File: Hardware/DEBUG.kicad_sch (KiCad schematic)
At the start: 0 parts

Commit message: Checkpoint
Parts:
- added J11: STDC14, leptunKicadLib:FTSH-107-01-L-DV-K-A, symbol Connector_Generic:Conn_02x07_Odd_Even
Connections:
- new net GND: J11.5 (Pin_5), J11.7 (Pin_7)
- new net T_JCLK/T_SWCLK: J11.6 (Pin_6), J11.9 (Pin_9)
- new net T_JTDI: J11.10 (Pin_10)
- new net T_JTDO/T_SWO: J11.8 (Pin_8)
- new net T_JTMS/T_SWDIO: J11.4 (Pin_4)
- new net T_NRST : J11.12 (Pin_12)
- new net T_VCC: J11.3 (Pin_3)
- new net T_VCP_RX: J11.13 (Pin_13)
- new net T_VCP_TX: J11.14 (Pin_14)
- no-connect marks 0 -> 3
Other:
- note added: "GNDDetect"
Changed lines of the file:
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@@
 (kicad_sch (version 20230121) (generator eeschema)
   (paper "A4")
-  (hierarchical_label "SWCLK" (shape bidirectional) (at 101.6 83.82 0) (fields_autoplaced)
+  (junction (at 154.94 91.44) (diameter 0) (color 0 0 0 0)
+  )
+  (junction (at 137.16 93.98) (diameter 0) (color 0 0 0 0)
+  )
+  (no_connect (at 124.46 99.06))
+  (no_connect (at 152.4 86.36))
+  (no_connect (at 139.7 86.36))
+  (wire (pts (xy 134.62 101.6) (xy 139.7 101.6))
+    (stroke (width 0) (type default))
+  )
+  (wire (pts (xy 137.16 91.44) (xy 139.7 91.44))
+    (stroke (width 0) (type default))
+  )
+  (wire (pts (xy 157.48 96.52) (xy 152.4 96.52))
+    (stroke (width 0) (type default))
+  )
+  (wire (pts (xy 137.16 93.98) (xy 139.7 93.98))
+    (stroke (width 0) (type default))
+  )
+  (wire (pts (xy 154.94 91.44) (xy 152.4 91.44))
+    (stroke (width 0) (type default))
+  )
+  (wire (pts (xy 157.48 91.44) (xy 154.94 91.44))
+    (stroke (width 0) (type default))
+  )
+  (wire (pts (xy 137.16 91.44) (xy 137.16 93.98))
+    (stroke (width 0) (type default))
+  )
+  (wire (pts (xy 124.46 99.06) (xy 139.7 99.06))
+    (stroke (width 0) (type default))
+  )
+  (wire (pts (xy 157.48 99.06) (xy 152.4 99.06))
+    (stroke (width 0) (type default))
+  )
+  (wire (pts (xy 134.62 93.98) (xy 137.16 93.98))
+    (stroke (width 0) (type default))
+  )
+  (wire (pts (xy 157.48 101.6) (xy 152.4 101.6))
+    (stroke (width 0) (type default))
+  )
+  (wire (pts (xy 137.16 104.14) (xy 154.94 104.14))
+    (stroke (width 0) (type default))
+  )
+  (wire (pts (xy 157.48 88.9) (xy 152.4 88.9))
+    (stroke (width 0) (type default))
+  )
+  (wire (pts (xy 139.7 96.52) (xy 137.16 96.52))
+    (stroke (width 0) (type default))
+  )
+  (wire (pts (xy 157.48 93.98) (xy 152.4 93.98))
+    (stroke (width 0) (type default))
+  )
+  (wire (pts (xy 137.16 96.52) (xy 137.16 104.14))
+    (stroke (width 0) (type default))
+  )
+  (wire (pts (xy 154.94 104.14) (xy 154.94 91.44))
+    (stroke (width 0) (type default))
+  )
+  (wire (pts (xy 134.62 88.9) (xy 139.7 88.9))
+    (stroke (width 0) (type default))
+  )
+  (text "GNDDetect" (at 124.46 99.06 0)
+    (effects (font (size 1.27 1.27)) (justify left bottom))
+  )
+  (hierarchical_label "T_JTMS{slash}T_SWDIO" (shape bidirectional) (at 157.48 88.9 0) (fields_autoplaced)
     (effects (font (size 1.27 1.27)) (justify left))
   )
-  (hierarchical_label "~{NRST}" (shape bidirectional) (at 101.6 78.74 0) (fields_autoplaced)
+  (hierarchical_label "T_JTDO{slash}T_SWO" (shape input) (at 157.48 93.98 0) (fields_autoplaced)
     (effects (font (size 1.27 1.27)) (justify left))
   )
-  (hierarchical_label "VCP_TX" (shape output) (at 101.6 88.9 0) (fields_autoplaced)
+  (hierarchical_label "T_NRST " (shape bidirectional) (at 157.48 99.06 0) (fields_autoplaced)
     (effects (font (size 1.27 1.27)) (justify left))
   )
-  (hierarchical_label "VCP_RX" (shape input) (at 101.6 91.44 0) (fields_autoplaced)
+  (hierarchical_label "T_VCC" (shape passive) (at 134.62 88.9 180) (fields_autoplaced)
+    (effects (font (size 1.27 1.27)) (justify right))
+  )
+  (hierarchical_label "T_JCLK{slash}T_SWCLK" (shape output) (at 157.48 91.44 0) (fields_autoplaced)
     (effects (font (size 1.27 1.27)) (justify left))
   )
-  (hierarchical_label "SWDIO" (shape bidirectional) (at 101.6 81.28 0) (fields_autoplaced)
+  (hierarchical_label "T_VCP_TX" (shape input) (at 157.48 101.6 0) (fields_autoplaced)
     (effects (font (size 1.27 1.27)) (justify left))
   )
-  (hierarchical_label "SWO" (shape bidirectional) (at 101.6 86.36 0) (fields_autoplaced)
+  (hierarchical_label "T_VCP_RX" (shape output) (at 134.62 101.6 180) (fields_autoplaced)
+    (effects (font (size 1.27 1.27)) (justify right))
+  )
+  (hierarchical_label "T_JTDI" (shape output) (at 157.48 96.52 0) (fields_autoplaced)
     (effects (font (size 1.27 1.27)) (justify left))
   )
+  (symbol (lib_id "Connector_Generic:Conn_02x07_Odd_Even") (at 144.78 93.98 0) (unit 1)
+    (in_bom yes) (on_board yes) (dnp no) (fields_autoplaced)
+    (property "Reference" "J11" (at 146.05 80.01 0)
+      (effects (font (size 1.27 1.27)))
+    )
+    (property "Value" "STDC14" (at 146.05 82.55 0)
+      (effects (font (size 1.27 1.27)))
+    )
+    (property "Footprint" "leptunKicadLib:FTSH-107-01-L-DV-K-A" (at 144.78 93.98 0)
+      (effects (font (size 1.27 1.27)) hide)
+    )
+    (property "Datasheet" "~" (at 144.78 93.98 0)
+      (effects (font (size 1.27 1.27)) hide)
+    )
+    (pin "1")
+    (pin "10")
+    (pin "11")
+    (pin "12")
+    (pin "13")
+    (pin "14")
+    (pin "2")
+    (pin "3")
+    (pin "4")
+    (pin "5")
+    (pin "6")
+    (pin "7")
+    (pin "8")
+    (pin "9")
+    (instances
+      (project "STM32_144_dev_board1"
+        (path "/687cb9d5-0148-4d02-92a8-2c8817ac4452/35098096-b805-4417-bb98-610cb63f0a62"
+          (reference "J11") (unit 1)
+        )
+      )
+      (project "Avionus_Flight_Controller"
+        (path "/ddc7e940-0588-4587-8902-8ced9e615ace/453e0de3-49a0-4fb1-b102-d46554d86fe8"
+          (reference "J1") (unit 1)
+        )
+      )
+    )
+  )
+  (symbol (lib_id "power:GND") (at 134.62 93.98 270) (unit 1)
+    (in_bom yes) (on_board yes) (dnp no) (fields_autoplaced)
+    (property "Reference" "#PWR067" (at 128.27 93.98 0)
+      (effects (font (size 1.27 1.27)) hide)
+    )
+    (property "Value" "GND" (at 130.81 93.9799 90)
+      (effects (font (size 1.27 1.27)) (justify right))
+    )
+    (property "Footprint" "" (at 134.62 93.98 0)
+      (effects (font (size 1.27 1.27)) hide)
+    )
+    (property "Datasheet" "" (at 134.62 93.98 0)
+      (effects (font (size 1.27 1.27)) hide)
+    )
+    (pin "1")
+    (instances
+      (project "STM32_144_dev_board1"
+        (path "/687cb9d5-0148-4d02-92a8-2c8817ac4452/35098096-b805-4417-bb98-610cb63f0a62"
+          (reference "#PWR067") (unit 1)
+        )
+      )
+      (project "Avionus_Flight_Controller"
+        (path "/ddc7e940-0588-4587-8902-8ced9e615ace/453e0de3-49a0-4fb1-b102-d46554d86fe8"
+          (reference "#PWR02") (unit 1)
+        )
+      )
+    )
+  )
 )

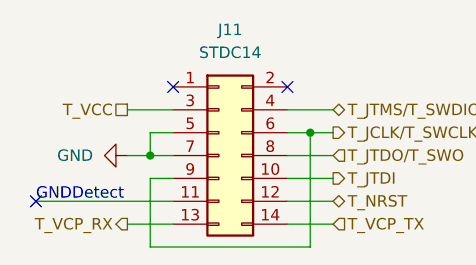
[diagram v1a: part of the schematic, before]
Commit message: ERC fixes
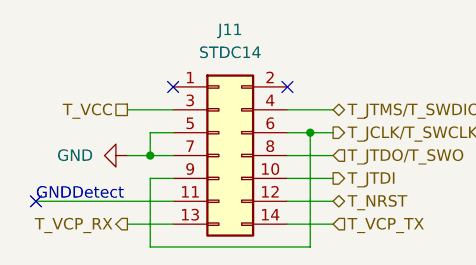
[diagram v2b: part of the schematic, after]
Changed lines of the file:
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@@
     (effects (font (size 1.27 1.27)) (justify left))
+  )
+  (symbol (lib_id "power:GND") (at 134.62 93.98 270) (unit 1)
+    (in_bom yes) (on_board yes) (dnp no) (fields_autoplaced)
+    (property "Reference" "#PWR02" (at 128.27 93.98 0)
+      (effects (font (size 1.27 1.27)) hide)
+    )
+    (property "Value" "GND" (at 130.81 93.98 90)
+      (effects (font (size 1.27 1.27)) (justify right))
+    )
+    (property "Footprint" "" (at 134.62 93.98 0)
+      (effects (font (size 1.27 1.27)) hide)
+    )
+    (property "Datasheet" "" (at 134.62 93.98 0)
+      (effects (font (size 1.27 1.27)) hide)
+    )
+    (pin "1")
+    (instances
+      (project "Avionus_Flight_Controller"
+        (path "/ddc7e940-0588-4587-8902-8ced9e615ace/453e0de3-49a0-4fb1-b102-d46554d86fe8"
+          (reference "#PWR02") (unit 1)
+        )
+      )
+    )
   )
   (symbol (lib_id "Connector_Generic:Conn_02x07_Odd_Even") (at 144.78 93.98 0) (unit 1)
@@
         )
       )
-    )
-  )
-  (symbol (lib_id "power:GND") (at 134.62 93.98 270) (unit 1)
-    (in_bom yes) (on_board yes) (dnp no) (fields_autoplaced)
-    (property "Reference" "#PWR067" (at 128.27 93.98 0)
-      (effects (font (size 1.27 1.27)) hide)
-    )
-    (property "Value" "GND" (at 130.81 93.9799 90)
-      (effects (font (size 1.27 1.27)) (justify right))
-    )
-    (property "Footprint" "" (at 134.62 93.98 0)
-      (effects (font (size 1.27 1.27)) hide)
-    )
-    (property "Datasheet" "" (at 134.62 93.98 0)
-      (effects (font (size 1.27 1.27)) hide)
-    )
-    (pin "1")
-    (instances
-      (project "STM32_144_dev_board1"
-        (path "/687cb9d5-0148-4d02-92a8-2c8817ac4452/35098096-b805-4417-bb98-610cb63f0a62"
-          (reference "#PWR067") (unit 1)
-        )
-      )
-      (project "Avionus_Flight_Controller"
-        (path "/ddc7e940-0588-4587-8902-8ced9e615ace/453e0de3-49a0-4fb1-b102-d46554d86fe8"
-          (reference "#PWR02") (unit 1)
-        )
-      )

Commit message: Checkpoint
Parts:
- renumbered J11 to J?
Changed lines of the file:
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@@
   (symbol (lib_id "power:GND") (at 134.62 93.98 270) (unit 1)
     (in_bom yes) (on_board yes) (dnp no) (fields_autoplaced)
-    (property "Reference" "#PWR02" (at 128.27 93.98 0)
+    (property "Reference" "#PWR0401" (at 128.27 93.98 0)
       (effects (font (size 1.27 1.27)) hide)
     )
@@
       (project "Avionus_Flight_Controller"
         (path "/ddc7e940-0588-4587-8902-8ced9e615ace/453e0de3-49a0-4fb1-b102-d46554d86fe8"
-          (reference "#PWR02") (unit 1)
+          (reference "#PWR0401") (unit 1)
         )
       )
@@
   (symbol (lib_id "Connector_Generic:Conn_02x07_Odd_Even") (at 144.78 93.98 0) (unit 1)
     (in_bom yes) (on_board yes) (dnp no) (fields_autoplaced)
-    (property "Reference" "J11" (at 146.05 80.01 0)
+    (property "Reference" "J?" (at 146.05 80.01 0)
       (effects (font (size 1.27 1.27)))
     )
@@
       (project "STM32_144_dev_board1"
         (path "/687cb9d5-0148-4d02-92a8-2c8817ac4452/35098096-b805-4417-bb98-610cb63f0a62"
-          (reference "J11") (unit 1)
+          (reference "J?") (unit 1)
         )
       )
       (project "Avionus_Flight_Controller"
         (path "/ddc7e940-0588-4587-8902-8ced9e615ace/453e0de3-49a0-4fb1-b102-d46554d86fe8"
-          (reference "J1") (unit 1)
+          (reference "J401") (unit 1)
         )
       )

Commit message: Checkpoint
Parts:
- added U401, U402: USBLC6-4SC6, Package_TO_SOT_SMD:SOT-23-6, symbol Power_Protection:USBLC6-4SC6
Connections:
- net GND: now also U401.2 (GND), U402.2 (GND)
- net T_JCLK/T_SWCLK: now also U402.6 (I/O4)
- net T_JTDI: now also U402.1 (I/O1)
- net T_JTDO/T_SWO: now also U402.3 (I/O2)
- net T_JTMS/T_SWDIO: now also U402.4 (I/O3)
- net T_NRST : now also U401.4 (I/O3)
- net T_VCC: now also U401.5 (VBUS), U402.5 (VBUS)
- net T_VCP_RX: now also U401.3 (I/O2)
- net T_VCP_TX: now also U401.6 (I/O4)
- net GNDDetect: now reaches J?.11 (Pin_11)
- net GNDDetect: now also U401.1 (I/O1)
- no-connect marks 3 -> 2
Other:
- note removed: "GNDDetect"
- moved on the sheet: J?

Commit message: Checkpoint routing
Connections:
- net GNDDetect: now also U402.1 (I/O1); no longer U401.1 (I/O1)
- net T_JCLK/T_SWCLK: now also U402.4 (I/O3); no longer U402.6 (I/O4)
- net T_JTDI: now also U401.4 (I/O3); no longer U402.1 (I/O1)
- net T_JTDO/T_SWO: now also U402.6 (I/O4); no longer U402.3 (I/O2)
- net T_JTMS/T_SWDIO: now also U402.3 (I/O2); no longer U402.4 (I/O3)
- net T_NRST : now also U401.6 (I/O4); no longer U401.4 (I/O3)
- net T_VCP_RX: now also U401.1 (I/O1); no longer U401.3 (I/O2)
- net T_VCP_TX: now also U401.3 (I/O2); no longer U401.6 (I/O4)
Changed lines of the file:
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@@
     (effects (font (size 1.27 1.27)) (justify left))
   )
-  (hierarchical_label "GNDDetect" (shape output) (at 162.56 71.12 180) (fields_autoplaced)
+  (hierarchical_label "GNDDetect" (shape output) (at 162.56 109.22 180) (fields_autoplaced)
     (effects (font (size 1.27 1.27)) (justify right))
   )
-  (hierarchical_label "T_VCP_RX" (shape output) (at 162.56 76.2 180) (fields_autoplaced)
+  (hierarchical_label "T_VCP_RX" (shape output) (at 162.56 71.12 180) (fields_autoplaced)
     (effects (font (size 1.27 1.27)) (justify right))
   )
-  (hierarchical_label "T_JTDI" (shape output) (at 162.56 109.22 180) (fields_autoplaced)
-    (effects (font (size 1.27 1.27)) (justify right))
+  (hierarchical_label "T_JTDI" (shape output) (at 182.88 71.12 0) (fields_autoplaced)
+    (effects (font (size 1.27 1.27)) (justify left))
   )
   (hierarchical_label "GNDDetect" (shape output) (at 96.52 99.06 180) (fields_autoplaced)
@@
     (effects (font (size 1.27 1.27)) (justify right))
   )
-  (hierarchical_label "T_VCP_TX" (shape input) (at 182.88 76.2 0) (fields_autoplaced)
-    (effects (font (size 1.27 1.27)) (justify left))
+  (hierarchical_label "T_VCP_TX" (shape input) (at 162.56 76.2 180) (fields_autoplaced)
+    (effects (font (size 1.27 1.27)) (justify right))
   )
-  (hierarchical_label "T_JTMS{slash}T_SWDIO" (shape bidirectional) (at 182.88 109.22 0) (fields_autoplaced)
-    (effects (font (size 1.27 1.27)) (justify left))
+  (hierarchical_label "T_JTMS{slash}T_SWDIO" (shape bidirectional) (at 162.56 114.3 180) (fields_autoplaced)
+    (effects (font (size 1.27 1.27)) (justify right))
   )
   (hierarchical_label "T_JCLK{slash}T_SWCLK" (shape output) (at 119.38 91.44 0) (fields_autoplaced)
@@
     (effects (font (size 1.27 1.27)) (justify right))
   )
-  (hierarchical_label "T_JTDO{slash}T_SWO" (shape input) (at 162.56 114.3 180) (fields_autoplaced)
-    (effects (font (size 1.27 1.27)) (justify right))
+  (hierarchical_label "T_JTDO{slash}T_SWO" (shape input) (at 182.88 114.3 0) (fields_autoplaced)
+    (effects (font (size 1.27 1.27)) (justify left))
   )
   (hierarchical_label "T_VCC" (shape passive) (at 172.72 101.6 90) (fields_autoplaced)
@@
     (effects (font (size 1.27 1.27)) (justify left))
   )
-  (hierarchical_label "T_NRST " (shape bidirectional) (at 182.88 71.12 0) (fields_autoplaced)
+  (hierarchical_label "T_NRST " (shape bidirectional) (at 182.88 76.2 0) (fields_autoplaced)
     (effects (font (size 1.27 1.27)) (justify left))
   )
-  (hierarchical_label "T_JCLK{slash}T_SWCLK" (shape output) (at 182.88 114.3 0) (fields_autoplaced)
+  (hierarchical_label "T_JCLK{slash}T_SWCLK" (shape output) (at 182.88 109.22 0) (fields_autoplaced)
     (effects (font (size 1.27 1.27)) (justify left))
   )

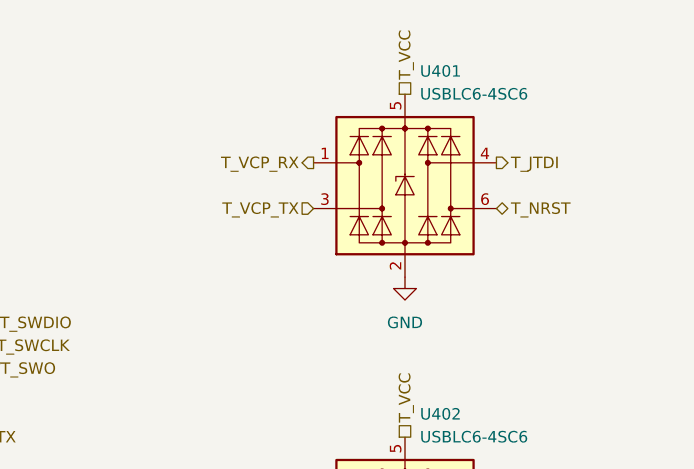
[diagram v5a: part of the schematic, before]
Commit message: Add lidar2
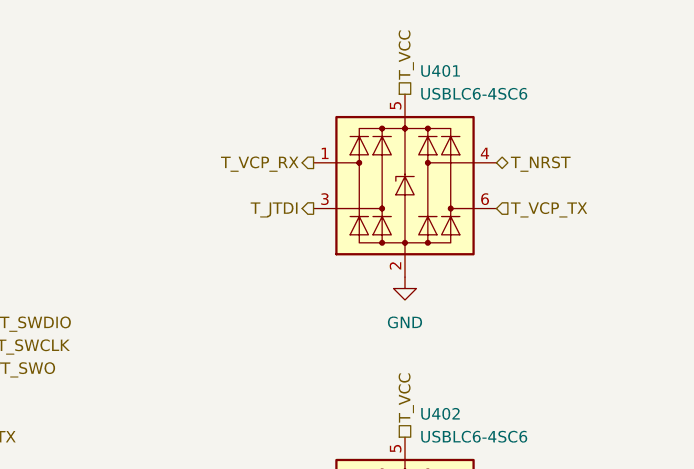
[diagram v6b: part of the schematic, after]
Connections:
- net T_JTDI: now also U401.3 (I/O2); no longer U401.4 (I/O3)
- net T_NRST : now also U401.4 (I/O3); no longer U401.6 (I/O4)
- net T_VCP_TX: now also U401.6 (I/O4); no longer U401.3 (I/O2)
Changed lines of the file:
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@@
     (effects (font (size 1.27 1.27)) (justify right))
   )
-  (hierarchical_label "T_JTDI" (shape output) (at 182.88 71.12 0) (fields_autoplaced)
-    (effects (font (size 1.27 1.27)) (justify left))
+  (hierarchical_label "T_JTDI" (shape output) (at 162.56 76.2 180) (fields_autoplaced)
+    (effects (font (size 1.27 1.27)) (justify right))
   )
   (hierarchical_label "GNDDetect" (shape output) (at 96.52 99.06 180) (fields_autoplaced)
@@
     (effects (font (size 1.27 1.27)) (justify right))
   )
-  (hierarchical_label "T_VCP_TX" (shape input) (at 162.56 76.2 180) (fields_autoplaced)
-    (effects (font (size 1.27 1.27)) (justify right))
+  (hierarchical_label "T_VCP_TX" (shape input) (at 182.88 76.2 0) (fields_autoplaced)
+    (effects (font (size 1.27 1.27)) (justify left))
   )
   (hierarchical_label "T_JTMS{slash}T_SWDIO" (shape bidirectional) (at 162.56 114.3 180) (fields_autoplaced)
@@
     (effects (font (size 1.27 1.27)) (justify left))
   )
-  (hierarchical_label "T_NRST " (shape bidirectional) (at 182.88 76.2 0) (fields_autoplaced)
+  (hierarchical_label "T_NRST " (shape bidirectional) (at 182.88 71.12 0) (fields_autoplaced)
     (effects (font (size 1.27 1.27)) (justify left))
   )

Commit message: Finalize silkscreen
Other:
- title: (none) -> Avionus_Flight_Controller
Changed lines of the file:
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@@
 (kicad_sch (version 20230121) (generator eeschema)
   (paper "A4")
+  (title_block
+    (title "Avionus_Flight_Controller")
+    (date "2023-11-25")
+    (rev "1.0")
+  )
   (junction (at 116.84 91.44) (diameter 0) (color 0 0 0 0)
   )
